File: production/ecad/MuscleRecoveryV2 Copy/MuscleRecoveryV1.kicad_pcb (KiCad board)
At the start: 2 copper layers, 50.7 x 55.6 mm, 99 parts, among them IC1 LC709203FQH-01TWG, J2 Conn_01x02, J3 Motor_Screw_Terminal, J4 USB_C_Receptacle_HRO_TYPE-C-3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, J5 SJ1-3533NG, J7 51296-1894, Q1 FDN340P, Q2 AO3400A, Q3 AO3400A, Q4 AO3400A, U1 AP1117-33, U2 MCP73831-2-OT, U3 CP2102N-Axx-xQFN28, U5 AD8232ACPZ-R7, U6 ESP32-WROOM-32E__16MB_, U7 ADS1115IDGS

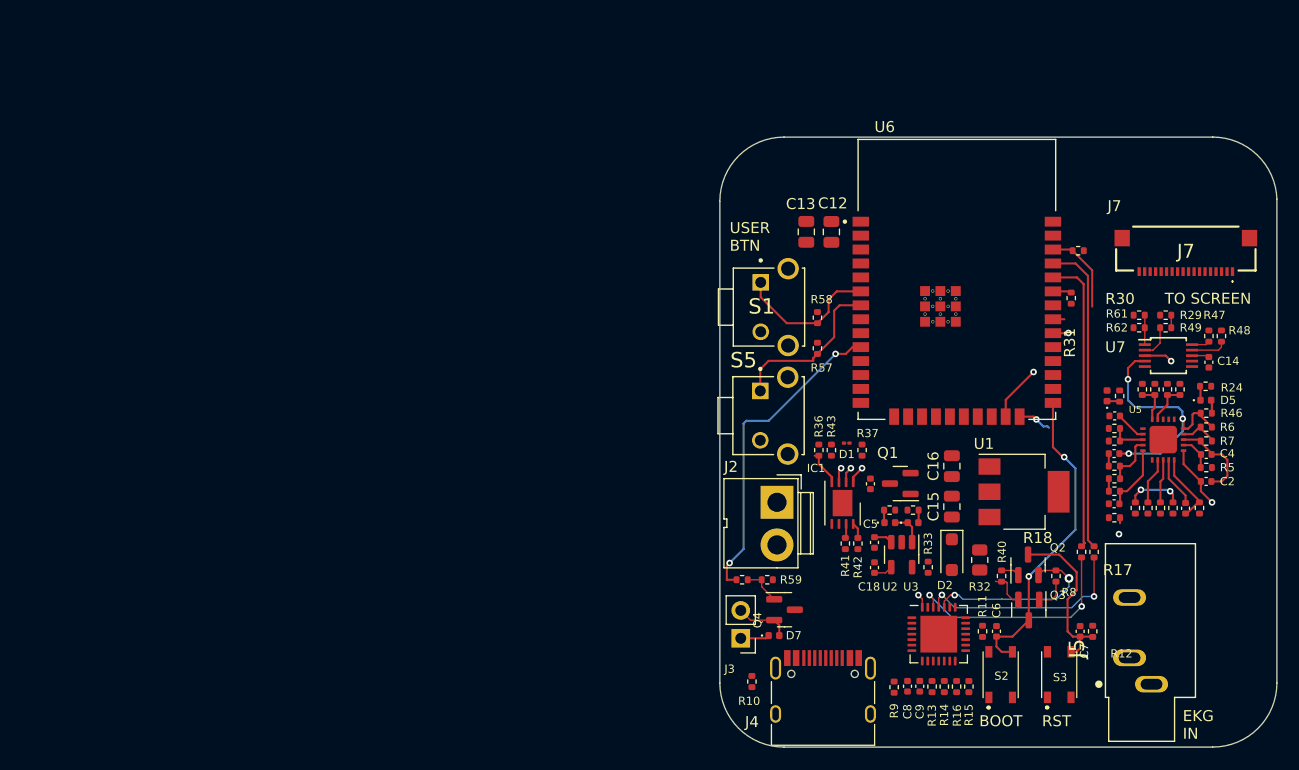
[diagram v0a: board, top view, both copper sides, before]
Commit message: Adding additional components to library for final rev2 changes
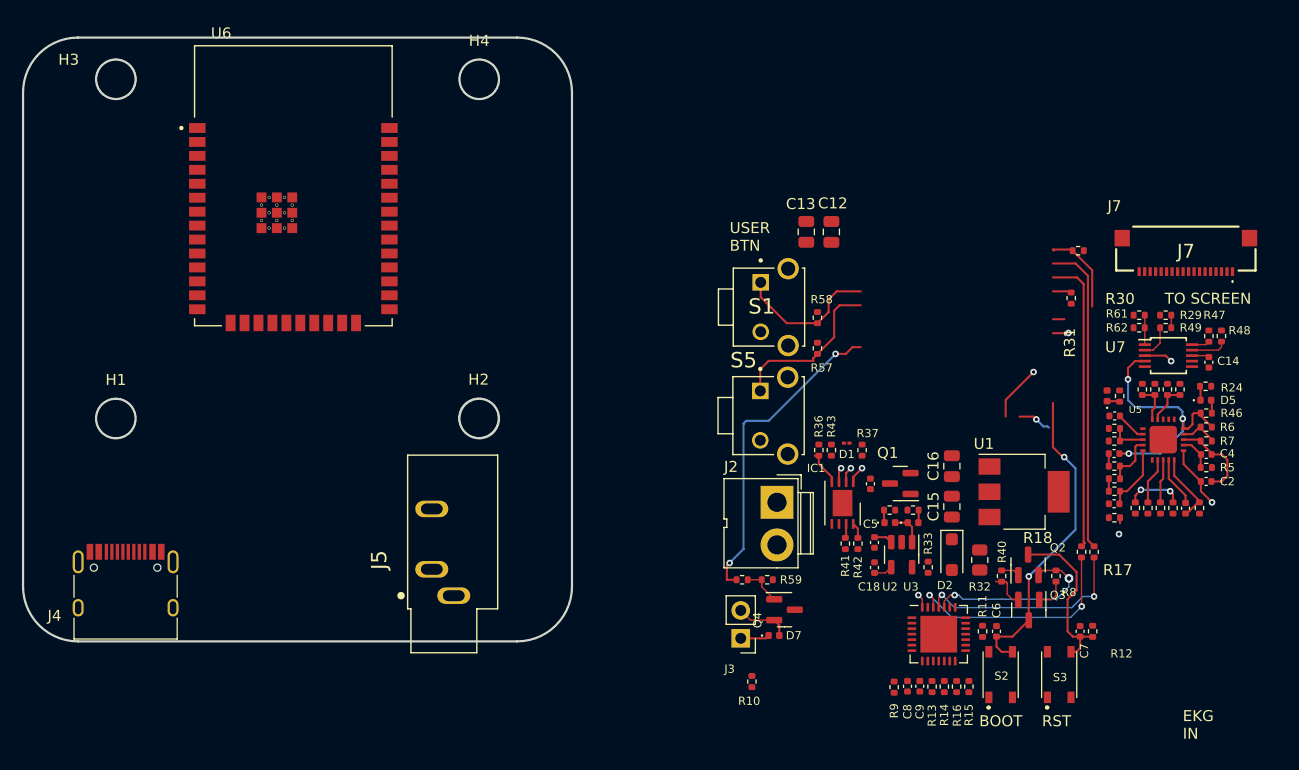
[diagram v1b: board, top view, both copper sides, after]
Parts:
- added H1: MountingHole, Muscle_Recovery_Footprint_Library:MH, F.Cu at (113.5, 83.6)
- added H2: MountingHole, Muscle_Recovery_Footprint_Library:MH, F.Cu at (146.6, 83.6)
- added H3: MountingHole, Muscle_Recovery_Footprint_Library:MH, F.Cu at (113.5, 52.7)
- added H4: MountingHole, Muscle_Recovery_Footprint_Library:MH, F.Cu at (146.6, 52.7)
- moved J4 64.3 mm to (114.4, 99.8)
- moved J5 64.1 mm to (144.3, 99.7)
- moved U6 61.0 mm to (129.7, 62.4)
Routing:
- net SDA: track 7.82 -> 1.55 mm
- net SCL: track 1.55 -> 7.82 mm
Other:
- board size 50.7 x 55.6 mm -> 50 x 55 mm

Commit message: Adding more updates to Rev2 Layout
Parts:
- added BT1: 3034, Muscle_Recovery_Footprint_Library:BAT_3034, F.Cu at (255.2, 51.9)
- added IC2: W25Q128JVPIQ, Muscle_Recovery_Footprint_Library:SON127P600X500X80-9N-D, B.Cu at (98.8, 126.6)
- added LS1: PKLCS1212E4001-R1, Muscle_Recovery_Footprint_Library:SPKR_PKLCS1212E4001-R1, B.Cu at (225.8, 43.4)
- added U4: PCF8523T/1_118, Muscle_Recovery_Footprint_Library:SO8_SOT96-1_NXP, B.Cu at (116.8, 120.6)
- J7: moved to B.Cu
- moved D7 94.0 mm to (86.5, 139.2)
- moved J3 94.0 mm to (83.5, 139.5)
- moved Q4 94.0 mm to (87.5, 136.9)
- moved J2 91.7 mm to (87.3, 122.0)
- moved C2 91.1 mm to (129.3, 125.5)
- moved R23 91.1 mm to (128.7, 127.9)
- moved C1 91.1 mm to (120.9, 127.6)
- moved C10 91.1 mm to (127.4, 128.0)
- moved C17 91.1 mm to (98.7, 125.7)
- moved C18 91.1 mm to (99.1, 133.4)
- moved C5 91.1 mm to (99.1, 131.1)
- moved C9 91.1 mm to (103.2, 144.2)
- moved D1 91.1 mm to (96.5, 122.0)
- moved D6 91.1 mm to (120.2, 117.7)
- moved IC1 91.1 mm to (96.1, 127.5)
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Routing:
- net TFT_DC: track 3.09 -> 0.00 mm, vias 1 -> 0
- net unconnected-(U4-*INT1/CLKOUT-Pad7): track 0.00 -> 3.09 mm, vias 0 -> 1
- net unconnected-(U6-NC1-Pad32): track 0.00 -> 1.67 mm, vias 0 -> 1
- net SCK: track 1.67 -> 0.00 mm, vias 1 -> 0
- net MISO: track 1.05 -> 0.00 mm
- net SCL: track 7.82 -> 8.87 mm
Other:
- outline, holes or cut-outs redrawn

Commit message: committing some recent changes to layout
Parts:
- removed BT1: 3034, Muscle_Recovery_Footprint_Library:BAT_3034
- removed J5: SJ1-3533NG, Muscle_Recovery_Footprint_Library:CUI_SJ1-3533NG
- removed R29: 4.7k, Resistor_SMD:R_0402_1005Metric
- removed R41, R42, R47, R48, R49: 0, Resistor_SMD:R_0402_1005Metric
- removed R61: DNP, Resistor_SMD:R_0402_1005Metric
- removed S1, S5: TL1105VF160Q, Muscle_Recovery_Footprint_Library:SW_TL1105VF160Q
- added C19: 1uF, Capacitor_SMD:C_0402_1005Metric, B.Cu at (135.9, 52.9)
- added C20: 10pF, Capacitor_SMD:C_0402_1005Metric, B.Cu at (124.6, 79.6)
- added C21: 10pF, Capacitor_SMD:C_0402_1005Metric, B.Cu at (113.5, 78.9)
- added C22: 1uF, Capacitor_SMD:C_0402_1005Metric, B.Cu at (124.7, 69.3)
- added C23: 1uF, Capacitor_SMD:C_0402_1005Metric, B.Cu at (124.7, 67.3)
- added J1: S2B-PH-SM4-TB_LF__SN_, Muscle_Recovery_Footprint_Library:JST_S2B-PH-SM4-TB_LF__SN_, F.Cu at (162.4, 72.0)
- added J6: Screw_Terminal_01x03, Connector_PinHeader_2.54mm:PinHeader_1x03_P2.54mm_Horizontal, F.Cu at (229.1, 98.1)
- added J8: SM02B-SRSS-TB_LF__SN_, Muscle_Recovery_Footprint_Library:SM02B-SRSS-TB_LF__SN_, F.Cu at (157.9, 64.3)
- added R27: 10K, Resistor_SMD:R_0402_1005Metric, B.Cu at (141.8, 52.9)
- added R35: 10K, Resistor_SMD:R_0402_1005Metric, B.Cu at (139.8, 52.9)
- added R50: 10K, Resistor_SMD:R_0402_1005Metric, B.Cu at (137.8, 52.9)
- added Y1: ABS07-32.768KHZ-7-T, Muscle_Recovery_Footprint_Library:XTAL_ABS07-32.768KHZ-7-T, B.Cu at (119.6, 78.9)
- C1, C10, C11, C14, C15, C16, C17, C18, C2, C3, C4, C5, C6, C7, C8, C9, D1, D2, D3, D4, D5, D6, D7, IC1, Q1, Q2, Q3, Q4, R1, R10, R11, R12, R13, R14, R15, R16, R17, R18, R19, R2, R20, R21, R22, R23, R24, R25, R26, R28, R3, R30, R31, R32, R33, R36, R37, R38, R39, R4, R40, R43, R44, R45, R46, R5, R59, R6, R60, R62, R63, R64, R7, R8, R9, S2, S3, U1, U2, U3, U5, U7: moved to B.Cu
- H1, H2, H3, H4: footprint Muscle_Recovery_Footprint_Library:MH -> MountingHole:MountingHole_3.2mm_M3
- J2: value Conn_01x02 -> SM02B-SRSS-TB_LF__SN_; footprint Connector:JWT_A3963_1x02_P3.96mm_Vertical -> Muscle_Recovery_Footprint_Library:SM02B-SRSS-TB_LF__SN_
- J3: footprint Connector_PinHeader_2.54mm:PinHeader_1x02_P2.54mm_Vertical -> Muscle_Recovery_Footprint_Library:Motor_Conn; moved to B.Cu
- J4: value USB_C_Receptacle_HRO_TYPE-C-31-M-12 -> USB_C_Receptacle_USB2.0; footprint Connector_USB:USB_C_Receptacle_HRO_TYPE-C-31-M-12 -> Muscle_Recovery_Footprint_Library:USB4110-GF-A_GCT
- moved J3 165.2 mm to (205.1, 27.6), turned to -90 degrees
- moved D7 161.1 mm to (210.1, 35.9)
- moved Q4 160.9 mm to (213.4, 36.8)
- moved R60 155.8 mm to (210.1, 38.2)
- moved R59 154.7 mm to (210.1, 37.0), turned to 180 degrees
- moved LS1 122.9 mm to (104.3, 61.8)
- moved U5 105.2 mm to (160.8, 61.7), turned to -90 degrees
- moved H2 105.2 mm to (191.9, 51.4)
- moved H1 105.0 mm to (158.8, 51.6)
- moved J4 104.7 mm to (174.5, 84.1)
- moved IC1 104.0 mm to (177.1, 62.2), turned to 0 degrees
- moved R10 103.7 mm to (170.1, 80.6), turned to 180 degrees
- moved R11 103.2 mm to (190.9, 76.6), turned to 90 degrees
- moved C6 103.0 mm to (192.0, 76.6), turned to -90 degrees
- moved R13 102.7 mm to (182.6, 77.7), turned to -90 degrees
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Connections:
- IC1 pad 7: Net-(IC1-SDA) -> SDA
- IC1 pad 8: Net-(IC1-SCL) -> SCL
- IC2 pad 1: unconnected-(IC2-~{CS}-Pad1) -> SPI_CS_FLSH
- IC2 pad 2: unconnected-(IC2-DO_(IO1)-Pad2) -> MISO
- IC2 pad 3: unconnected-(IC2-~{WP_(IO2)}-Pad3) -> Net-(IC2-~{WP_(IO2)})
- IC2 pad 4: unconnected-(IC2-GND_1-Pad4) -> GND
- IC2 pad 5: unconnected-(IC2-DI_(IO0)-Pad5) -> MISO
- IC2 pad 6: unconnected-(IC2-CLK-Pad6) -> SCK
- IC2 pad 7: unconnected-(IC2-~{HOLD_OR_}/RESET_(IO3)-Pad7) -> Net-(IC2-~{HOLD_OR_}/RESET_(IO3))
- IC2 pad 8: unconnected-(IC2-VCC-Pad8) -> +3.3V
- IC2 pad 9: unconnected-(IC2-GND_2-Pad9) -> GND
- J2 pad 1: +BATT -> +3.3V
- J2 pad 2: GND -> ALT_START_BUTTON
- J4 pad A5: (no net) -> Net-(J4-CC1)
- J4 pad A6: (no net) -> USB-
- J4 pad A7: (no net) -> USB+
- J4 pad A8: (no net) -> unconnected-(J4-SBU1-PadA8)
- J4 pad B5: (no net) -> Net-(J4-CC2)
- J4 pad B6: (no net) -> USB-
- J4 pad B7: (no net) -> USB+
- J4 pad B8: (no net) -> unconnected-(J4-SBU2-PadB8)
- J7 pad 10: LIT -> SD_CS
- J7 pad 2: GND -> LIT
- J7 pad 3: SCK -> GND
- J7 pad 4: MISO -> SCK
- J7 pad 6: TFT_CS -> MISO
- J7 pad 7: TFT_RST -> TFT_DC
- J7 pad 8: TFT_DC -> TFT_CS
- J7 pad 9: SD_CS -> TFT_RST
- LS1 pad N: unconnected-(LS1-PadN) -> GND
- LS1 pad P: unconnected-(LS1-PadP) -> SPKR
- U4 pad 1: unconnected-(U4-OSCI-Pad1) -> OSC1
- U4 pad 2: unconnected-(U4-OSCO-Pad2) -> OSC2
- U4 pad 3: unconnected-(U4-VBAT-Pad3) -> +BATT
- U4 pad 4: unconnected-(U4-VSS-Pad4) -> GND
- U4 pad 5: unconnected-(U4-SDA-Pad5) -> SDA
- U4 pad 6: unconnected-(U4-SCL-Pad6) -> SCL
- U4 pad 8: unconnected-(U4-VDD-Pad8) -> +3.3V
- U6 pad 12: IO27 -> SPKR
- U6 pad 8: IO32 -> SPI_CS_FLSH
- U7 pad 10: Net-(U7-SCL) -> SCL
- U7 pad 2: Net-(U7-ALERT/RDY) -> ALERT/READY
- U7 pad 9: Net-(U7-SDA) -> SDA
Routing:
- net EN: track 15.3 -> 60.7 mm, vias 0 -> 3
- net MOTOR_EN: track 29.3 -> 0.00 mm, vias 2 -> 0
- net TXD0: track 28.5 -> 0.00 mm
- net RXD0: track 27.1 -> 0.00 mm
- net /Bootloading/RXD: track 20.8 -> 0.00 mm, vias 2 -> 0
- net SCL: track 8.87 -> 29.7 mm, vias 0 -> 1
- net ALERT/READY: track 1.14 -> 21.4 mm, vias 0 -> 1
- net /Bootloading/TXD: track 19.6 -> 0.00 mm, vias 2 -> 0
- net Vout: track 24.0 -> 6.28 mm, vias 3 -> 2
- net DTR: track 4.75 -> 22.0 mm, vias 1 -> 0
- net IO0: track 28.7 -> 13.1 mm
- net START_BUTTON: track 15.1 -> 0.00 mm
- net RTS: track 16.8 -> 31.6 mm, vias 2 -> 0
- net USB+: track 0.00 -> 14.7 mm, vias 0 -> 1
- net USB-: track 0.00 -> 14.0 mm, vias 0 -> 1
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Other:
- board size 50 x 55 mm -> 42 x 39 mm
- board text added: "Peripherals on I2C"
- board text added: "SPI Peripherals"

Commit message: Pushing Most of the final changes for PCB REV2
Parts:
- removed J6: Screw_Terminal_01x03, Connector_PinHeader_2.54mm:PinHeader_1x03_P2.54mm_Horizontal
- removed LS1: PKLCS1212E4001-R1, Muscle_Recovery_Footprint_Library:SPKR_PKLCS1212E4001-R1
- removed R57, R58: 10k, Resistor_SMD:R_0402_1005Metric
- removed S2, S3: B3F-1000, Muscle_Recovery_Footprint_Library:PTS810SJG250SMTRLFS
- added C24: 1uF, Capacitor_SMD:C_0402_1005Metric, B.Cu at (176.3, 64.4)
- added C25: 0.1uF, Capacitor_SMD:C_0402_1005Metric, B.Cu at (172.1, 67.2)
- added J5: USB4110-GF-A, Muscle_Recovery_Footprint_Library:USB4110-GF-A_GCT, F.Cu at (174.5, 84.1)
- added R29: 10k, Resistor_SMD:R_0402_1005Metric, F.Cu at (160.5, 68.1)
- added R51: 10k, Resistor_SMD:R_0402_1005Metric, F.Cu at (187.1, 73.9)
- added U8: ADXL343, Package_LGA:LGA-14_3x5mm_P0.8mm_LayoutBorder1x6y, B.Cu at (175.7, 66.8)
- C13: moved to B.Cu
- D7: value LED_Small -> 1N914WT; footprint LED_SMD:LED_0402_1005Metric -> Diode_SMD:D_SOD-523; moved to F.Cu
- J2: value SM02B-SRSS-TB_LF__SN_ -> SM03B-SRSS-TB_LF__SN_; footprint Muscle_Recovery_Footprint_Library:SM02B-SRSS-TB_LF__SN_ -> Muscle_Recovery_Footprint_Library:JST_SM03B-SRSS-TB_LF__SN_
- J3: value Motor_Screw_Terminal -> SM02B-SRSS-TB_LF__SN_; footprint Muscle_Recovery_Footprint_Library:Motor_Conn -> Muscle_Recovery_Footprint_Library:SM02B-SRSS-TB_LF__SN_; moved to F.Cu
- J4: value USB_C_Receptacle_USB2.0 -> SM02B-SRSS-TB_LF__SN_; footprint Muscle_Recovery_Footprint_Library:USB4110-GF-A_GCT -> Muscle_Recovery_Footprint_Library:SM02B-SRSS-TB_LF__SN_
- Q4, R17, R18, R30, R31, R59, R60: moved to F.Cu
- moved C13 86.6 mm to (166.4, 57.0)
- moved C12 82.9 mm to (164.0, 56.5)
- moved R31 73.7 mm to (186.4, 58.7), turned to 0 degrees
- moved R30 68.9 mm to (186.4, 62.5), turned to 180 degrees
- moved C21 62.2 mm to (175.6, 76.1), turned to -90 degrees
- moved C22 54.5 mm to (178.9, 74.4), turned to -90 degrees
- moved R18 54.5 mm to (186.4, 59.9), turned to 180 degrees
- moved R50 53.5 mm to (187.8, 71.9)
- moved Y1 53.3 mm to (172.8, 76.5)
- moved C19 53.2 mm to (184.6, 74.2), turned to 180 degrees
- moved R17 52.8 mm to (186.4, 61.2), turned to 180 degrees
- moved IC2 50.6 mm to (183.5, 70.7), turned to 0 degrees
- moved C20 45.6 mm to (170.1, 76.2)
- moved C23 45.2 mm to (169.8, 70.6), turned to 90 degrees
- moved R27 45.0 mm to (181.4, 74.3), turned to 180 degrees
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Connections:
- C16 pad 1: +3.3V -> +3V3
- C19 pad 1: +3.3V -> +3V3
- C22 pad 1: +3.3V -> +3V3
- C8 pad 1: +3.3V -> +3V3
- C9 pad 1: +3.3V -> +3V3
- D7 pad 1: +3.3V -> +3V3
- IC2 pad 5: MISO -> MOSI
- IC2 pad 8: +3.3V -> +3V3
- J2 pad 1: +3.3V -> RL
- J2 pad 2: ALT_START_BUTTON -> LA
- J2 pad 3: (no net) -> RA
- J3 pad 1: +3.3V -> +3V3
- J7 pad 1: +3.3V -> unconnected-(J7-Pad1)
- J7 pad 10: SD_CS -> TFT_RST
- J7 pad 11: unconnected-(J7-Pad11) -> TFT_CS
- J7 pad 12: unconnected-(J7-Pad12) -> TFT_DC
- J7 pad 13: unconnected-(J7-Pad13) -> MISO
- J7 pad 14: unconnected-(J7-Pad14) -> MOSI
- J7 pad 15: unconnected-(J7-Pad15) -> SCK
- J7 pad 16: unconnected-(J7-Pad16) -> GND
- J7 pad 17: unconnected-(J7-Pad17) -> LIT
- J7 pad 18: unconnected-(J7-Pad18) -> +3V3
- J7 pad 2: LIT -> unconnected-(J7-Pad2)
- J7 pad 3: GND -> unconnected-(J7-Pad3)
- J7 pad 4: SCK -> unconnected-(J7-Pad4)
- J7 pad 5: MOSI -> unconnected-(J7-Pad5)
- J7 pad 6: MISO -> unconnected-(J7-Pad6)
- J7 pad 7: TFT_DC -> unconnected-(J7-Pad7)
- J7 pad 8: TFT_CS -> unconnected-(J7-Pad8)
- J7 pad 9: TFT_RST -> SD_CS
- J8 pad 1: +3.3V -> +3V3
- Q4 pad 2: Net-(D7-A) -> GND
- Q4 pad 3: GND -> Net-(D7-A)
- R10 pad 1: Net-(J4-CC1) -> Net-(J5-CC1)
- R11 pad 1: +3.3V -> +3V3
- R12 pad 1: +3.3V -> +3V3
- R16 pad 1: +3.3V -> +3V3
- R27 pad 1: +3.3V -> +3V3
- R35 pad 1: +3.3V -> +3V3
- R50 pad 1: +3.3V -> +3V3
- R9 pad 1: Net-(J4-CC2) -> Net-(J5-CC2)
- U1 pad 2: +3.3V -> +3V3
- U3 pad 6: +3.3V -> +3V3
- U3 pad 7: +3.3V -> +3V3
- U4 pad 8: +3.3V -> +3V3
- U6 pad 10: MOTOR_EN -> unconnected-(U6-IO25-Pad10)
- U6 pad 11: IO26 -> ALT_START_BUTTON
- U6 pad 26: Net-(U6-IO4) -> TFT_RST
- U6 pad 27: unconnected-(U6-IO16-Pad27) -> START_BUTTON
- U6 pad 28: unconnected-(U6-IO17-Pad28) -> MOTOR_EN
- U6 pad 6: ALT_START_BUTTON -> unconnected-(U6-IO34-Pad6)
- U6 pad 7: START_BUTTON -> unconnected-(U6-IO35-Pad7)
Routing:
- net GND: track 1.02 -> 83.9 mm, vias 0 -> 54
- net +3V3: track 2.99 -> 61.5 mm, vias 0 -> 25
- net +BATT: track 1.71 -> 49.0 mm, vias 0 -> 3
- net /Bootloading/RXD: track 0.00 -> 43.8 mm, vias 0 -> 3
- net /Bootloading/TXD: track 0.00 -> 40.4 mm, vias 0 -> 1
- net SD_CS: track 0.00 -> 32.6 mm, vias 0 -> 1
- net SPI_CS_FLSH: track 0.00 -> 30.7 mm, vias 0 -> 1
- net MOSI: track 0.00 -> 28.7 mm, vias 0 -> 1
- net LIT: track 0.00 -> 28.6 mm, vias 0 -> 1
- net MISO: track 0.00 -> 23.2 mm, vias 0 -> 2
- net TFT_RST: track 0.00 -> 21.3 mm, vias 0 -> 1
- net Vout: track 6.28 -> 26.8 mm
- net TFT_CS: track 0.00 -> 19.7 mm, vias 0 -> 1
- net TFT_DC: track 0.00 -> 18.4 mm, vias 0 -> 1
- net SCK: track 0.00 -> 18.4 mm, vias 0 -> 3
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- added copper zone on In1.Cu, net +3V3
- added copper zone on In1.Cu, net +BATT
- added copper zone on F.Cu, net GND
- added copper zone on In2.Cu, net GND
- added copper zone on In1.Cu, net VBUS
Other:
- copper layers 2 -> 4
- board text added: "Abrego A. | Fox W. Tong M. | Tong M. Ahn R. | Yoon B."
- board text added: "BATT IN"
- board text added: "BUT1 IN"
- board text added: "BUT2 IN"
- board text added: "MOTOR OUT"
- board text added: "REV 2 - Muscle Recovery S 24'"
- board text added: "SCREEN OUT"
- board text added: "Serial Number:"
- board text removed: "BOOT"
- board text removed: "J7"
- board text removed: "Peripherals on I2C"
- board text removed: "RST"
- board text removed: "SPI Peripherals"
- board text removed: "TO SCREEN"
- board text removed: "USER BTN"

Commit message: Pushing changes post schematic review
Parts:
- removed D1: GREEN, Inductor_SMD:L_01005_0402Metric
- removed IC1: LC709203FQH-01TWG, Package_DFN_QFN:WDFN-8-1EP_4x3mm_P0.65mm_EP2.4x1.8mm
- removed R36: 10K, Resistor_SMD:R_0402_1005Metric
- removed R43: 0, Resistor_SMD:R_0402_1005Metric
- added R34: 100, Resistor_SMD:R_0402_1005Metric, B.Cu at (172.2, 60.8)
- added U9: MAX17043G+T, Muscle_Recovery_Footprint_Library:21-0174B_MXM-L, B.Cu at (175.3, 61.3)
- R37: value 10K -> 1k
- moved R37 2.24 mm to (172.2, 62.0)
- moved C17 2.14 mm to (172.2, 63.1)
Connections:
- R37 pad 1: Net-(D1-K) -> +BATT
- R37 pad 2: GND -> Net-(U9-CELL)
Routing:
- net SW: track 15.6 -> 23.6 mm
- net +BATT: track 49.0 -> 43.8 mm
- net Net-(IC1-~{ALARMB}): track 2.90 -> 0.00 mm
- net SCL: track 32.6 -> 34.0 mm, vias 1 -> 2
- net Net-(U9-CELL): track 0.00 -> 1.33 mm
- net Net-(U9-VDD): track 0.00 -> 1.27 mm
- net Net-(D1-A): track 1.20 -> 0.00 mm
- net Net-(D1-K): track 1.20 -> 0.00 mm
- net SDA: track 28.7 -> 29.8 mm
- net GND: track 83.9 -> 84.9 mm
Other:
- board text added: "Pin 1"

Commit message: Pushing final Rev2 PCBA Files
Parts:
- removed R44: DNP, Resistor_SMD:R_0402_1005Metric
- removed R45, R63, R64: 0, Resistor_SMD:R_0402_1005Metric
- added R24: 1K, Resistor_SMD:R_0402_1005Metric, B.Cu at (161.7, 65.7)
- added TP1: TestPoint, TestPoint:TestPoint_Pad_1.0x1.0mm, B.Cu at (171.7, 85.2)
- added TP2: TestPoint, TestPoint:TestPoint_Pad_1.0x1.0mm, F.Cu at (163.6, 80.9)
- added TP3: TestPoint, TestPoint:TestPoint_Pad_1.0x1.0mm, F.Cu at (187.8, 78.6)
- added TP4: TestPoint, TestPoint:TestPoint_Pad_1.0x1.0mm, F.Cu at (192.3, 56.9)
- added TP5: TestPoint, TestPoint:TestPoint_Pad_1.0x1.0mm, F.Cu at (189.5, 56.9)
- added TP8: TestPoint, TestPoint:TestPoint_Pad_1.0x1.0mm, B.Cu at (175.5, 85.2)
- added TP9: TestPoint, TestPoint:TestPoint_Pad_1.0x1.0mm, F.Cu at (170.7, 77.3)
- moved R3 1.65 mm to (161.7, 66.7)
- moved C13 0.25 mm to (166.6, 57.0)
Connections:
- J2 pad S2: unconnected-(J2-SHIELD-PadS1) -> unconnected-(J2-SHIELD-PadS2)
- R20 pad 2: Net-(U5-FR) -> +3V3
- R21 pad 2: Net-(U5-FR) -> +3V3
- R30 pad 2: SCL -> SDA
- R31 pad 1: SDA -> SCL
- U5 pad 14: Net-(U5-AC/*DC) -> GND
- U5 pad 15: Net-(U5-FR) -> +3V3
- U5 pad GND: (no net) -> GND
- U6 pad 12: SPKR -> unconnected-(U6-IO27-Pad12)
- U6 pad 14: ALERT/READY -> unconnected-(U6-IO12-Pad14)
- U6 pad 33: SCL -> SDA
- U6 pad 36: SDA -> SCL
- U6 pad 9: IO33 -> unconnected-(U6-IO33-Pad9)
- U7 pad 2: ALERT/READY -> unconnected-(U7-ALERT/RDY-Pad2)
- U8 pad 7: unconnected-(U8-~{CS}-Pad7) -> +3V3
- U9 pad 6: unconnected-(U9-QSRT-Pad6) -> GND
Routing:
- net ALERT/READY: track 22.7 -> 0.00 mm, vias 1 -> 0
- net Net-(R1-Pad2): track 1.14 -> 23.5 mm, vias 0 -> 2
- net SDA: track 29.8 -> 46.8 mm
- net Net-(U5-FR): track 13.1 -> 0.00 mm, vias 2 -> 0
- net GND: track 84.9 -> 96.5 mm, vias 54 -> 53
- net +3V3: track 61.4 -> 71.6 mm, vias 25 -> 32
- net SW: track 23.6 -> 15.5 mm
- net +BATT: track 43.8 -> 51.2 mm, vias 3 -> 6
- net Net-(U5-AC/*DC): track 4.13 -> 0.00 mm
- net SCL: track 34.0 -> 37.8 mm
- net VBUS: track 16.7 -> 20.4 mm
- net SDN: track 0.00 -> 2.67 mm
- net Net-(J5-CC2): track 7.66 -> 6.28 mm, vias 2 -> 1
- net USB-: track 14.0 -> 14.9 mm
- net USB+: track 14.7 -> 15.4 mm
- added copper zone on B.Cu, net +3V3
- added copper zone on F.Cu, net +BATT
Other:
- board text added: "Abrego A. | Fox W. Tong M. | Ahn R. Yoon B."
- board text added: "REV 2: Muscle Recovery S 24'"
- board text removed: "Abrego A. | Fox W. Tong M. | Tong M. Ahn R. | Yoon B."
- board text removed: "Pin 1"
- board text removed: "REV 2 - Muscle Recovery S 24'"
